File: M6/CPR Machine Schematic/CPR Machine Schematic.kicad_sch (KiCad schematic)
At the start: 0 parts

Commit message: More Schematics
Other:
- added sheet HMI (HMI.kicad_sch)
- added sheet Microcontroller (Microcontroller.kicad_sch)
- added sheet Motor Control (MotorControl.kicad_sch)
- added sheet Power (Power.kicad_sch)
- added sheet Sensing (Sensing.kicad_sch)

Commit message: ToF
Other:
- sheet Microcontroller ports: added SPI_CS, SPI_INT, SPI_SCK, SPI_SDI, SPI_SDO; removed CS, INT, SCK, SDI, SDO
- sheet Motor Control ports: added SPI_CS, SPI_INT, SPI_SCK, SPI_SDI, SPI_SDO; removed CS, INT, SCK, SDI, SDO
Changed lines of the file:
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@@
 			)
 		)
-		(pin "SCK" input
+		(pin "SPI_SCK" input
 			(at 86.36 87.63 0)
 			(effects
@@
 			)
 		)
-		(pin "SDI" input
+		(pin "SPI_SDI" input
 			(at 86.36 91.44 0)
 			(effects
@@
 			)
 		)
-		(pin "SDO" output
+		(pin "SPI_SDO" output
 			(at 86.36 95.25 0)
 			(effects
@@
 			)
 		)
-		(pin "CS" input
+		(pin "SPI_CS" input
 			(at 86.36 99.06 0)
 			(effects
@@
 			)
 		)
-		(pin "INT" output
+		(pin "SPI_INT" output
 			(at 86.36 102.87 0)
 			(effects
@@
 			)
 		)
-		(pin "INT" input
+		(pin "SPI_INT" input
 			(at 113.03 102.87 180)
 			(effects
@@
 			)
 		)
-		(pin "CS" output
+		(pin "SPI_CS" output
 			(at 113.03 99.06 180)
 			(effects
@@
 			)
 		)
-		(pin "SDI" output
+		(pin "SPI_SDI" output
 			(at 113.03 91.44 180)
 			(effects
@@
 			)
 		)
-		(pin "SDO" input
+		(pin "SPI_SDO" input
 			(at 113.03 95.25 180)
 			(effects
@@
 			)
 		)
-		(pin "SCK" output
+		(pin "SPI_SCK" output
 			(at 113.03 87.63 180)
 			(effects

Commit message: morer kicad
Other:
- sheet HMI ports: added UART_RX, UART_TX; removed none
- sheet Microcontroller ports: added I2C_SCL, I2C_SDA, UART_RX, UART_TX; removed none
- sheet Sensing ports: added I2C_SCL, I2C_SDA; removed none
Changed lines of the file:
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@@
+	(wire
+		(pts
+			(xy 152.4 87.63) (xy 177.8 87.63)
+		)
+		(stroke
+			(width 0)
+			(type default)
+		)
+	)
 	(wire
 		(pts
@@
 	(wire
 		(pts
+			(xy 87.63 132.08) (xy 113.03 132.08)
+		)
+		(stroke
+			(width 0)
+			(type default)
+		)
+	)
+	(wire
+		(pts
+			(xy 87.63 135.89) (xy 113.03 135.89)
+		)
+		(stroke
+			(width 0)
+			(type default)
+		)
+	)
+	(wire
+		(pts
 			(xy 86.36 99.06) (xy 113.03 99.06)
 		)
@@
 		(pts
 			(xy 86.36 91.44) (xy 113.03 91.44)
+		)
+		(stroke
+			(width 0)
+			(type default)
+		)
+	)
+	(wire
+		(pts
+			(xy 152.4 91.44) (xy 177.8 91.44)
 		)
 		(stroke
@@
 	(sheet
 		(at 35.56 125.73)
-		(size 51.435 27.94)
+		(size 53.34 27.94)
 		(exclude_from_sim no)
 		(in_bom yes)
@@
 			)
 		)
+		(pin "I2C_SCL" input
+			(at 88.9 132.08 0)
+			(effects
+				(font
+					(size 1.27 1.27)
+				)
+				(justify right)
+			)
+		)
+		(pin "I2C_SDA" bidirectional
+			(at 88.9 135.89 0)
+			(effects
+				(font
+					(size 1.27 1.27)
+				)
+				(justify right)
+			)
+		)
 		(instances
 			(project "CPR Machine Schematic"
@@
 	)
 	(sheet
-		(at 36.195 36.83)
-		(size 52.07 26.67)
+		(at 35.56 36.83)
+		(size 53.34 26.67)
 		(exclude_from_sim no)
 		(in_bom yes)
@@
 		)
 		(property "Sheetname" "Power"
-			(at 36.195 36.1184 0)
+			(at 35.56 36.1184 0)
 			(effects
 				(font
@@
 		)
 		(property "Sheetfile" "Power.kicad_sch"
-			(at 36.195 64.0846 0)
+			(at 35.56 64.0846 0)
 			(effects
 				(font
@@
 	)
 	(sheet
-		(at 35.56 78.105)
-		(size 50.8 37.465)
+		(at 35.56 78.74)
+		(size 53.34 36.83)
 		(exclude_from_sim no)
 		(in_bom yes)
@@
 		)
 		(property "Sheetname" "Motor Control"
-			(at 35.56 77.3934 0)
+			(at 35.56 78.0284 0)
 			(effects
 				(font
@@
 		)
 		(pin "SPI_SCK" input
-			(at 86.36 87.63 0)
+			(at 88.9 87.63 0)
 			(effects
 				(font
@@
 		)
 		(pin "SPI_SDI" input
-			(at 86.36 91.44 0)
+			(at 88.9 91.44 0)
 			(effects
 				(font
@@
 		)
 		(pin "SPI_SDO" output
-			(at 86.36 95.25 0)
+			(at 88.9 95.25 0)
 			(effects
 				(font
@@
 		)
 		(pin "SPI_CS" input
-			(at 86.36 99.06 0)
+			(at 88.9 99.06 0)
 			(effects
 				(font
@@
 		)
 		(pin "SPI_INT" output
-			(at 86.36 102.87 0)
+			(at 88.9 102.87 0)
 			(effects
 				(font
@@
 	)
 	(sheet
-		(at 175.895 78.105)
-		(size 41.275 37.465)
+		(at 177.8 78.74)
+		(size 39.37 36.83)
 		(exclude_from_sim no)
 		(in_bom yes)
@@
 		)
 		(property "Sheetname" "HMI"
-			(at 175.895 77.3934 0)
+			(at 177.8 78.0284 0)
 			(effects
 				(font
@@
 		)
 		(property "Sheetfile" "HMI.kicad_sch"
-			(at 175.895 116.1546 0)
+			(at 177.8 116.1546 0)
 			(effects
 				(font
@@
 				)
 				(justify left top)
+			)
+		)
+		(pin "UART_RX" input
+			(at 177.8 91.44 180)
+			(effects
+				(font
+					(size 1.27 1.27)
+				)
+				(justify left)
+			)
+		)
+		(pin "UART_TX" output
+			(at 177.8 87.63 180)
+			(effects
+				(font
+					(size 1.27 1.27)
+				)
+				(justify left)
 			)
 		)
@@
 	(sheet
 		(at 113.03 78.74)
-		(size 41.275 74.93)
+		(size 39.37 74.93)
 		(exclude_from_sim no)
 		(in_bom yes)
@@
 			)
 		)
+		(pin "I2C_SDA" bidirectional
+			(at 113.03 135.89 180)
+			(effects
+				(font
+					(size 1.27 1.27)
+				)
+				(justify left)
+			)
+		)
+		(pin "I2C_SCL" output
+			(at 113.03 132.08 180)
+			(effects
+				(font
+					(size 1.27 1.27)
+				)
+				(justify left)
+			)
+		)
+		(pin "UART_TX" output
+			(at 152.4 91.44 0)
+			(effects
+				(font
+					(size 1.27 1.27)
+				)
+				(justify right)
+			)
+		)
+		(pin "UART_RX" input
+			(at 152.4 87.63 0)
+			(effects
+				(font
+					(size 1.27 1.27)
+				)
+				(justify right)
+			)
+		)

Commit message: HMI schem for real for real
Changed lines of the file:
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@@
 	(wire
 		(pts
-			(xy 86.36 102.87) (xy 113.03 102.87)
+			(xy 88.9 91.44) (xy 113.03 91.44)
 		)
 		(stroke
@@
 	(wire
 		(pts
-			(xy 86.36 87.63) (xy 113.03 87.63)
+			(xy 88.9 132.08) (xy 113.03 132.08)
 		)
 		(stroke
@@
 	(wire
 		(pts
-			(xy 86.36 95.25) (xy 113.03 95.25)
+			(xy 88.9 87.63) (xy 113.03 87.63)
 		)
 		(stroke
@@
 	(wire
 		(pts
-			(xy 87.63 132.08) (xy 113.03 132.08)
+			(xy 88.9 135.89) (xy 113.03 135.89)
 		)
 		(stroke
@@
 	(wire
 		(pts
-			(xy 87.63 135.89) (xy 113.03 135.89)
+			(xy 88.9 102.87) (xy 113.03 102.87)
 		)
 		(stroke
@@
 	(wire
 		(pts
-			(xy 86.36 99.06) (xy 113.03 99.06)
+			(xy 88.9 95.25) (xy 113.03 95.25)
 		)
 		(stroke
@@
 	(wire
 		(pts
-			(xy 86.36 91.44) (xy 113.03 91.44)
+			(xy 88.9 99.06) (xy 113.03 99.06)
 		)
 		(stroke

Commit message: Finalized kiCAD
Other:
- sheet HMI renamed HMI_Raspi
- added sheet HMI_Teensy (HMI_Teensy.kicad_sch)
- sheet HMI_Raspi: file HMI.kicad_sch -> HMI_Raspi.kicad_sch
- sheet Microcontroller ports: added Green_Button, Green_LED, I2S_BCLK, I2S_DIN, I2S_LRC, RST1, RST2, Red_Button, Red_LED, SPI_CS2, SPI_CS3, White_Button; removed UART_RX, UART_TX

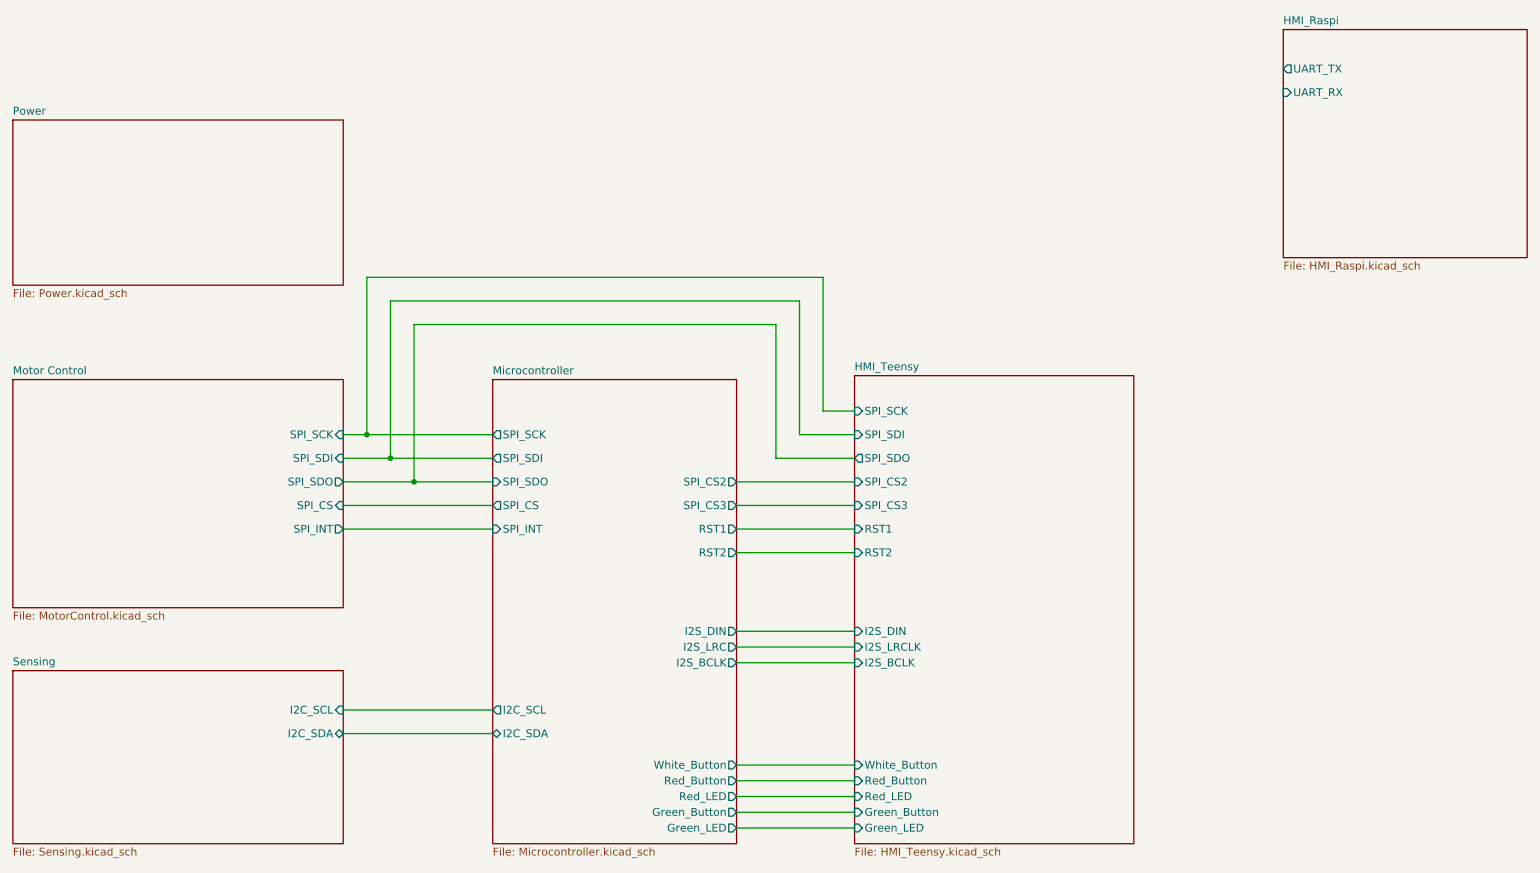
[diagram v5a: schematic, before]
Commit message: Single-pager KiCAD
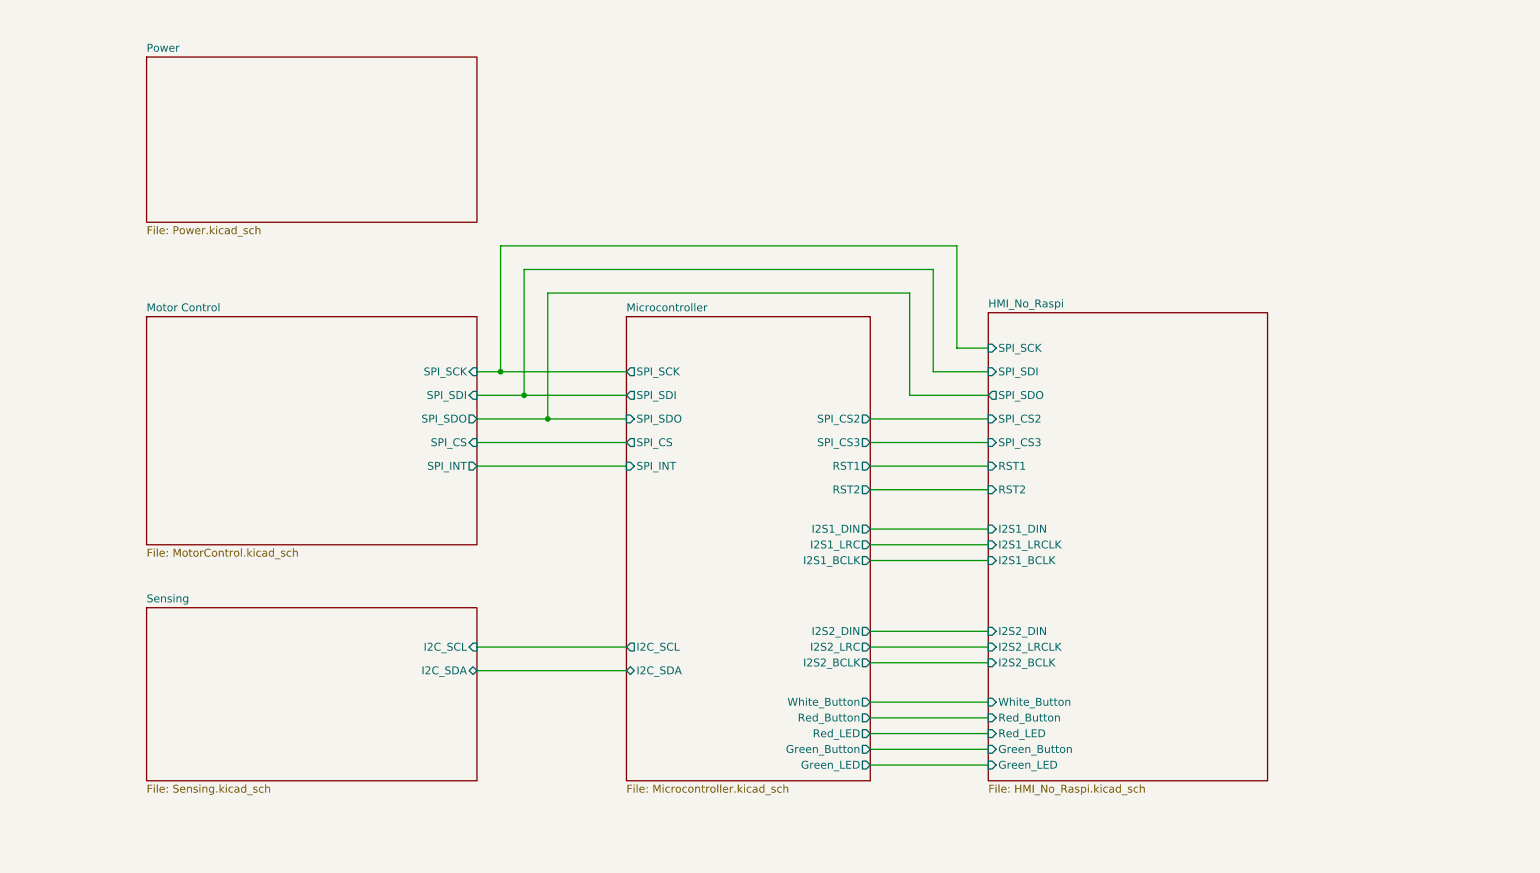
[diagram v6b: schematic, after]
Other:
- sheet HMI_Teensy renamed HMI_No_Raspi
- removed sheet HMI_Raspi
- sheet HMI_No_Raspi: file HMI_Teensy.kicad_sch -> HMI_No_Raspi.kicad_sch
- sheet HMI_No_Raspi ports: added I2S1_BCLK, I2S1_DIN, I2S1_LRCLK, I2S2_BCLK, I2S2_DIN, I2S2_LRCLK; removed I2S_BCLK, I2S_DIN, I2S_LRCLK
- sheet Microcontroller ports: added I2S1_BCLK, I2S1_DIN, I2S1_LRC, I2S2_BCLK, I2S2_DIN, I2S2_LRC; removed I2S_BCLK, I2S_DIN, I2S_LRC

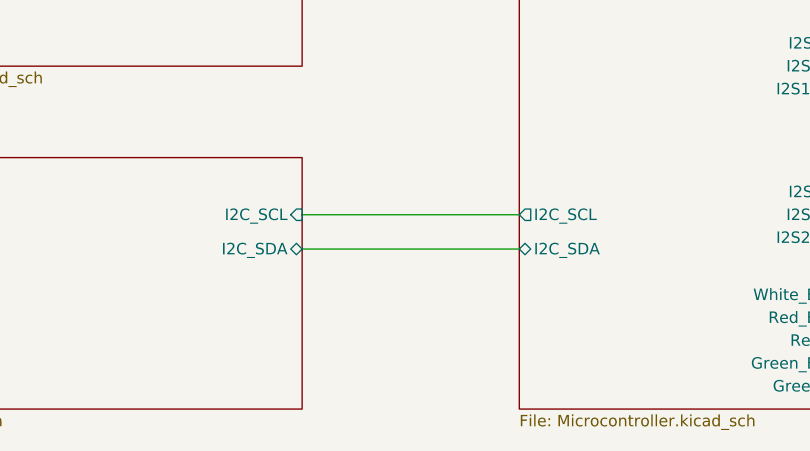
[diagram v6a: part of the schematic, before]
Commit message: force sensor oobs
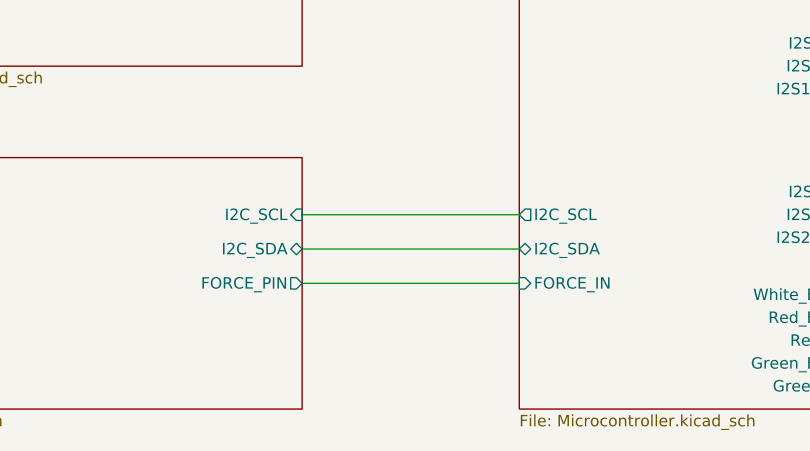
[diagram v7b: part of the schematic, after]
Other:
- sheet Microcontroller ports: added FORCE_IN; removed none
- sheet Sensing ports: added FORCE_PIN; removed none
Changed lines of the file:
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@@
+	(wire
+		(pts
+			(xy 110.49 129.54) (xy 134.62 129.54)
+		)
+		(stroke
+			(width 0)
+			(type default)
+		)
+	)
 	(wire
 		(pts
@@
 			)
 		)
+		(pin "FORCE_PIN" output
+			(at 110.49 129.54 0)
+			(effects
+				(font
+					(size 1.27 1.27)
+				)
+				(justify right)
+			)
+		)
 		(instances
 			(project "CPR Machine Schematic"
@@
 			)
 		)
+		(pin "FORCE_IN" input
+			(at 134.62 129.54 180)
+			(effects
+				(font
+					(size 1.27 1.27)
+				)
+				(justify left)
+			)
+		)

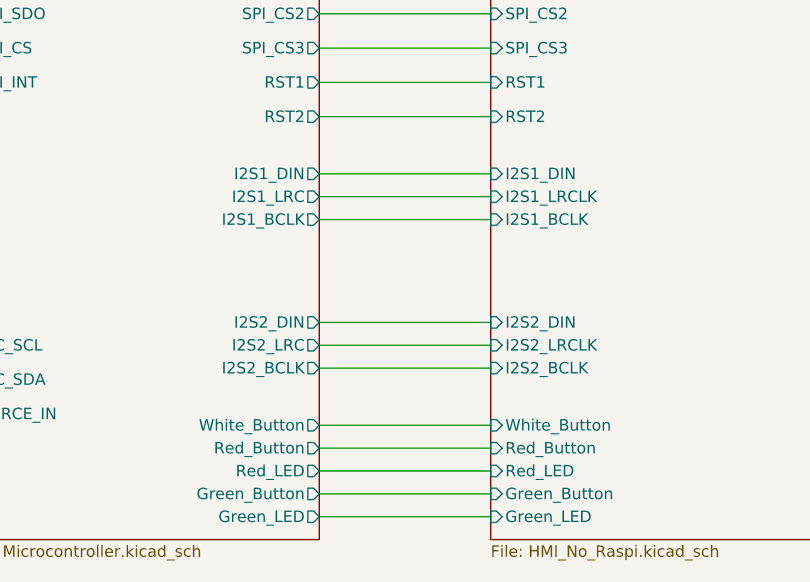
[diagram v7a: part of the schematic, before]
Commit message: I2S Combination and Screen driver fixes
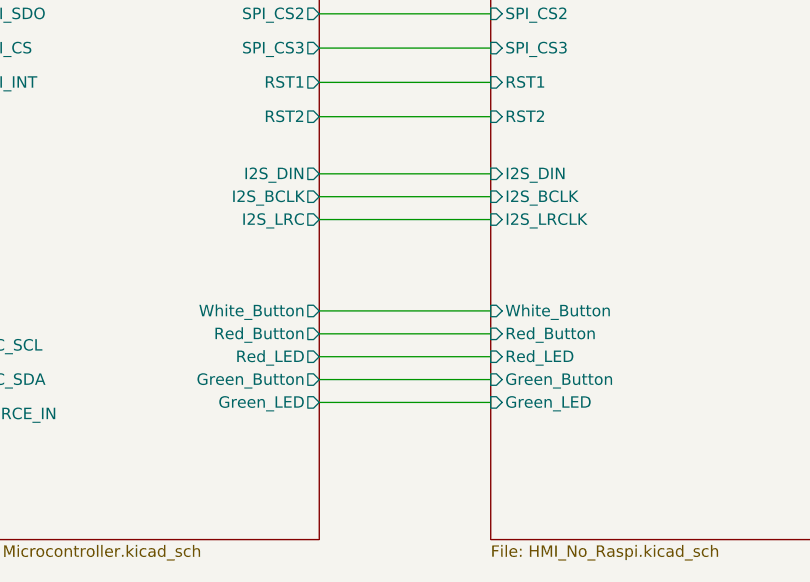
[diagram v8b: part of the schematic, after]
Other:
- sheet HMI_No_Raspi ports: added I2S_BCLK, I2S_DIN, I2S_LRCLK; removed I2S1_BCLK, I2S1_DIN, I2S1_LRCLK, I2S2_BCLK, I2S2_DIN, I2S2_LRCLK
- sheet Microcontroller ports: added I2S_BCLK, I2S_DIN, I2S_LRC; removed I2S1_BCLK, I2S1_DIN, I2S1_LRC, I2S2_BCLK, I2S2_DIN, I2S2_LRC
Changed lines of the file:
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@@
 	(wire
 		(pts
-			(xy 173.99 135.89) (xy 193.04 135.89)
+			(xy 173.99 123.19) (xy 193.04 123.19)
 		)
 		(stroke
@@
 	(wire
 		(pts
-			(xy 173.99 130.81) (xy 193.04 130.81)
+			(xy 173.99 118.11) (xy 193.04 118.11)
 		)
 		(stroke
@@
 	(wire
 		(pts
-			(xy 173.99 138.43) (xy 193.04 138.43)
+			(xy 173.99 125.73) (xy 193.04 125.73)
 		)
 		(stroke
@@
 	(wire
 		(pts
-			(xy 173.99 133.35) (xy 193.04 133.35)
-		)
-		(stroke
-			(width 0)
-			(type default)
-		)
-	)
-	(wire
-		(pts
-			(xy 173.99 140.97) (xy 193.04 140.97)
+			(xy 173.99 120.65) (xy 193.04 120.65)
+		)
+		(stroke
+			(width 0)
+			(type default)
+		)
+	)
+	(wire
+		(pts
+			(xy 173.99 128.27) (xy 193.04 128.27)
 		)
 		(stroke
@@
 	(wire
 		(pts
-			(xy 173.99 121.92) (xy 193.04 121.92)
-		)
-		(stroke
-			(width 0)
-			(type default)
-		)
-	)
-	(wire
-		(pts
 			(xy 121.92 85.09) (xy 134.62 85.09)
 		)
@@
 	(wire
 		(pts
-			(xy 173.99 124.46) (xy 193.04 124.46)
-		)
-		(stroke
-			(width 0)
-			(type default)
-		)
-	)
-	(wire
-		(pts
 			(xy 173.99 105.41) (xy 193.04 105.41)
-		)
-		(stroke
-			(width 0)
-			(type default)
-		)
-	)
-	(wire
-		(pts
-			(xy 173.99 119.38) (xy 193.04 119.38)
 		)
 		(stroke
@@
 		)
 		(pin "Green_Button" input
-			(at 193.04 138.43 180)
+			(at 193.04 125.73 180)
 			(effects
 				(font
@@
 		)
 		(pin "Green_LED" input
-			(at 193.04 140.97 180)
+			(at 193.04 128.27 180)
 			(effects
 				(font
@@
 		)
 		(pin "Red_Button" input
-			(at 193.04 133.35 180)
+			(at 193.04 120.65 180)
 			(effects
 				(font
@@
 		)
 		(pin "Red_LED" input
-			(at 193.04 135.89 180)
+			(at 193.04 123.19 180)
 			(effects
 				(font
@@
 		)
 		(pin "White_Button" input
-			(at 193.04 130.81 180)
+			(at 193.04 118.11 180)
 			(effects
 				(font
@@
 			)
 		)
-		(pin "I2S2_BCLK" input
-			(at 193.04 124.46 180)
-			(effects
-				(font
-					(size 1.27 1.27)
-				)
-				(justify left)
-			)
-		)
-		(pin "I2S2_LRCLK" input
-			(at 193.04 121.92 180)
-			(effects
-				(font
-					(size 1.27 1.27)
-				)
-				(justify left)
-			)
-		)
-		(pin "I2S2_DIN" input
-			(at 193.04 119.38 180)
-			(effects
-				(font
-					(size 1.27 1.27)
-				)
-				(justify left)
-			)
-		)
-		(pin "I2S1_LRCLK" input
+		(pin "I2S_LRCLK" input
+			(at 193.04 107.95 180)
+			(effects
+				(font
+					(size 1.27 1.27)
+				)
+				(justify left)
+			)
+		)
+		(pin "I2S_DIN" input
+			(at 193.04 102.87 180)
+			(effects
+				(font
+					(size 1.27 1.27)
+				)
+				(justify left)
+			)
+		)
+		(pin "I2S_BCLK" input
 			(at 193.04 105.41 180)
-			(effects
-				(font
-					(size 1.27 1.27)
-				)
-				(justify left)
-			)
-		)
-		(pin "I2S1_DIN" input
-			(at 193.04 102.87 180)
-			(effects
-				(font
-					(size 1.27 1.27)
-				)
-				(justify left)
-			)
-		)
-		(pin "I2S1_BCLK" input
-			(at 193.04 107.95 180)
 			(effects
 				(font
@@
 		)
 		(pin "Red_Button" output
-			(at 173.99 133.35 0)
+			(at 173.99 120.65 0)
 			(effects
 				(font
@@
 		)
 		(pin "White_Button" output
-			(at 173.99 130.81 0)
+			(at 173.99 118.11 0)
 			(effects
 				(font
@@
 		)
 		(pin "Green_Button" output
-			(at 173.99 138.43 0)
+			(at 173.99 125.73 0)
 			(effects
 				(font
@@
 		)
 		(pin "Green_LED" output
-			(at 173.99 140.97 0)
+			(at 173.99 128.27 0)
 			(effects
 				(font
@@
 		)
 		(pin "Red_LED" output
-			(at 173.99 135.89 0)
-			(effects
-				(font
-					(size 1.27 1.27)
-				)
-				(justify right)
-			)
-		)
-		(pin "I2S2_DIN" output
-			(at 173.99 119.38 0)
-			(effects
-				(font
-					(size 1.27 1.27)
-				)
-				(justify right)
-			)
-		)
-		(pin "I2S2_LRC" output
-			(at 173.99 121.92 0)
-			(effects
-				(font
-					(size 1.27 1.27)
-				)
-				(justify right)
-			)
-		)
-		(pin "I2S2_BCLK" output
-			(at 173.99 124.46 0)
-			(effects
-				(font
-					(size 1.27 1.27)
-				)
-				(justify right)
-			)
-		)
-		(pin "I2S1_BCLK" output
-			(at 173.99 107.95 0)
-			(effects
-				(font
-					(size 1.27 1.27)
-				)
-				(justify right)
-			)
-		)
-		(pin "I2S1_LRC" output
-			(at 173.99 105.41 0)
-			(effects
-				(font
-					(size 1.27 1.27)
-				)
-				(justify right)
-			)
-		)
-		(pin "I2S1_DIN" output
-			(at 173.99 102.87 0)
+			(at 173.99 123.19 0)
 			(effects
 				(font
@@
 			)
 		)
+		(pin "I2S_DIN" output
+			(at 173.99 102.87 0)
+			(effects
+				(font
+					(size 1.27 1.27)
+				)
+				(justify right)
+			)
+		)
+		(pin "I2S_LRC" output
+			(at 173.99 107.95 0)
+			(effects
+				(font
+					(size 1.27 1.27)
+				)
+				(justify right)
+			)
+		)
+		(pin "I2S_BCLK" output
+			(at 173.99 105.41 0)
+			(effects
+				(font
+					(size 1.27 1.27)
+				)
+				(justify right)
+			)
+		)
